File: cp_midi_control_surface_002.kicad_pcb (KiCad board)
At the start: 2 copper layers, 201 parts, among them P1 Power, P10 Guide, P11 Guide, P12 Guide, P13 Guide, P2 Analogue, P3 Digital, P4 Communication, P5 PWM, P6 PWM, P8 Guide, P9 Guide, SW1 B3F-5050, SW10 B3F-5050, SW11 B3F-5050, SW12 B3F-5050, SW13 B3F-5050, SW14 B3F-5050, SW15 B3F-5050, SW16 B3F-5050, SW17 B3F-5050, SW18 B3F-5050, SW19 B3F-5050, SW2 B3F-5050, SW20 B3F-5050, SW21 B3F-5050, SW22 B3F-5050, SW23 B3F-5050, SW24 B3F-5050, SW25 B3F-5050, SW26 B3F-5050, SW27 B3F-5050, SW28 B3F-5050, SW29 B3F-5050, SW3 B3F-5050, SW30 B3F-5050, SW31 B3F-5050, SW32 B3F-5050, SW33 B3F-5050, SW34 B3F-5050, SW35 B3F-5050, SW36 B3F-5050, SW37 B3F-5050, SW38 B3F-5050, SW39 B3F-5050, SW4 B3F-5050, SW40 B3F-5050, SW41 B3F-5050, SW42 B3F-5050, SW43 B3F-5050, SW44 B3F-5050, SW45 B3F-5050, SW46 B3F-5050, SW47 B3F-5050, SW48 B3F-5050, SW49 B3F-5050, SW5 B3F-5050, SW50 B3F-5050, SW51 B3F-5050, SW52 B3F-5050, SW53 B3F-5050, SW54 B3F-5050, SW55 B3F-5050, SW56 B3F-5050, SW6 B3F-5050, SW7 B3F-5050, SW8 B3F-5050, SW9 B3F-5050, U1 CD74HC4067M, U2 CD74HC4067M, U3 CD74HC4067M, U4 CD74HC4067M, U5 CD74HC4067M, U6 CD74HC4067M

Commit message: Resize boards and update connector
Resized the boards to fit the new modular height and started changing the interboard connectors
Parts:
- removed H1, H10, H11, H12, H13, H14, H15, H16, H17, H18, H19, H2, H20, H21, H22, H23, H24, H25, H26, H3, H4, H5, H6, H7, H8, H9: ~, cunabulapress-footprints:Mounting_Hole_M3_with_Target
- removed P10: Guide, cunabulapress-footprints:Mounting_Hole_M3_Target_Only
- removed REF**: Clearance_Hole_M3, cunabulapress-footprints:Clearance_Hole_M3
- removed REF** (x4): Mounting_Hole_M3, cunabulapress-footprints:Mounting_Hole_M3_Target_Only
- J3: footprint cunabulapress-footprints:Connector_TE_Connectivity_Micro-MaTch_8_Position_Female -> Connector_PinHeader_2.54mm:PinHeader_1x06_P2.54mm_Vertical
- moved J3 26.4 mm to (210.4, 225.5), turned to 90 degrees

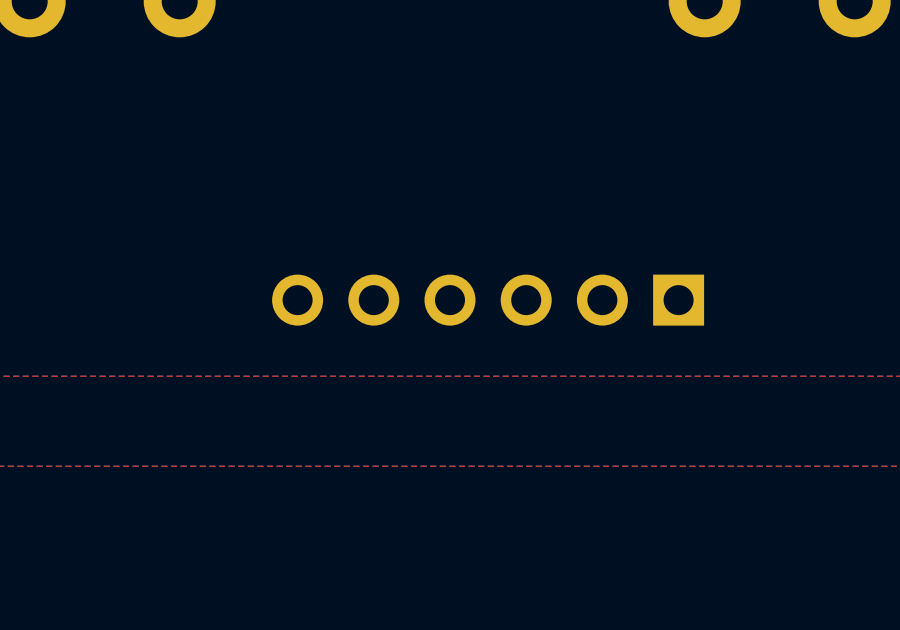
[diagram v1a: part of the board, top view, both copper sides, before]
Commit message: Added Rails to Layout
Found a big problem that the rails are compatible with the boards being modular the way the components are currently spaced.

Which is a little frustrating.
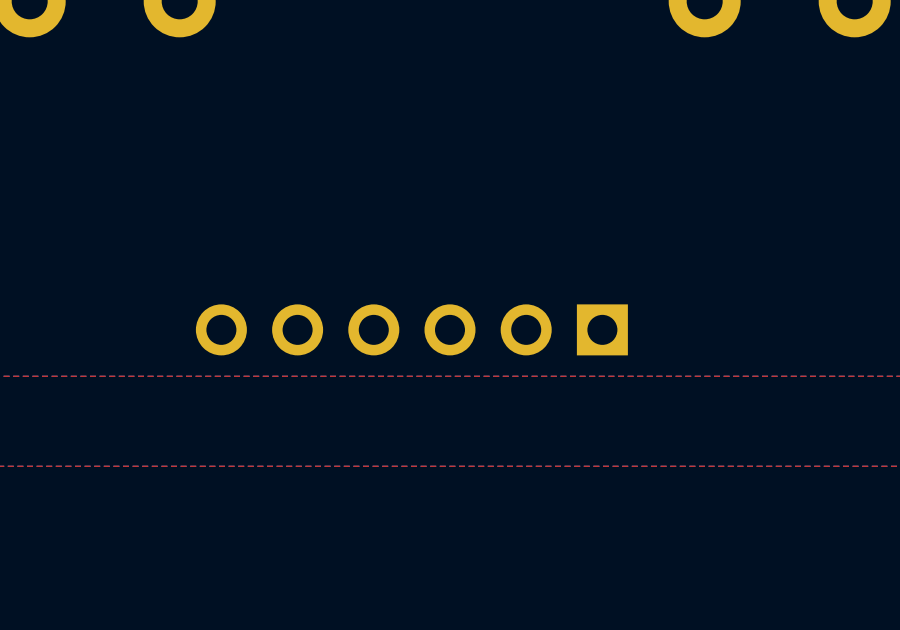
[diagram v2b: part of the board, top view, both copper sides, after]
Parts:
- moved J3 2.73 mm to (207.8, 226.5)

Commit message: COrrected the placement of most of the components for the modular design
Need to finalise the Arduino placement and work out the design for possible extensions.
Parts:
- removed J1, J2, J4, J5, J6, J7, J8: ~, cunabulapress-footprints:Connector_TE_Connectivity_Micro-MaTch_8_Position_Female
- removed J10, J12: ~, Connector_PinSocket_2.54mm:PinSocket_1x04_P2.54mm_Vertical
- removed J11, J9: ~, Connector_PinHeader_2.54mm:PinHeader_1x04_P2.54mm_Vertical
- removed J13, J15, J17, J19: ~, Connector_PinHeader_2.54mm:PinHeader_1x01_P2.54mm_Vertical
- removed J14, J16, J18, J20: ~, Connector_PinSocket_2.54mm:PinSocket_1x01_P2.54mm_Vertical
- removed J21, J23, J25, J27: ~, Connector_PinHeader_2.54mm:PinHeader_1x08_P2.54mm_Vertical
- removed J22, J24, J26, J28: ~, Connector_PinSocket_2.54mm:PinSocket_1x08_P2.54mm_Vertical
- removed J3: ~, Connector_PinHeader_2.54mm:PinHeader_1x06_P2.54mm_Vertical
- removed RN2, RN3: 680Ω (Bussed), Resistor_THT:R_Array_SIP9
- moved RN1 353.4 mm to (791.1, 328.0)
- moved SW_F1 353.4 mm to (768.2, 339.4)
- moved SW36 221.1 mm to (114.3, 264.2)
- moved SW35 220.8 mm to (137.2, 264.2)
- moved SW33 220.3 mm to (182.9, 264.2)
- moved SW40 220.0 mm to (205.7, 264.2)
- moved SW39 219.8 mm to (228.6, 264.2)
- moved SW34 219.7 mm to (160.0, 264.2)
- moved SW38 219.5 mm to (251.5, 264.2)
- moved SW37 219.3 mm to (274.3, 264.2)
- moved D16 188.4 mm to (393.7, 264.2)
- moved D15 188.3 mm to (388.1, 264.2)
- moved D14 188.3 mm to (382.5, 264.2)
- moved D13 188.2 mm to (376.9, 264.2)
- moved D12 188.2 mm to (371.3, 264.2)
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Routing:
- net +5V: track 2702.6 -> 0.00 mm, vias 1 -> 0
- net S3: track 522.6 -> 0.00 mm, vias 1 -> 0
- net S2: track 519.4 -> 0.00 mm, vias 1 -> 0
- net S0: track 516.2 -> 0.00 mm, vias 1 -> 0
- net S1: track 514.1 -> 0.00 mm, vias 1 -> 0
- net Net-(RV3-Pad2): track 481.2 -> 0.00 mm
- net Net-(RV2-Pad2): track 441.6 -> 0.00 mm, vias 1 -> 0
- net Net-(RV8-Pad2): track 401.0 -> 0.00 mm, vias 1 -> 0
- net Net-(RV7-Pad2): track 393.9 -> 0.00 mm, vias 1 -> 0
- net Net-(RV1-Pad2): track 391.8 -> 0.00 mm, vias 1 -> 0
- net Net-(RV6-Pad2): track 390.9 -> 0.00 mm, vias 1 -> 0
- net Net-(RV5-Pad2): track 389.5 -> 0.00 mm, vias 1 -> 0
- net Net-(RV4-Pad2): track 387.1 -> 0.00 mm, vias 1 -> 0
- net /13: track 369.0 -> 0.00 mm
- net /12: track 360.9 -> 0.00 mm
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- removed copper zone on B.Cu, net (none)
- removed copper zone on F.Cu, net (none)
- removed copper zone on B.Cu, net GND
- removed copper zone on F.Cu, net GND
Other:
- board outline added: 421.6 x 221 mm
- board text removed: "Alt Switch position"
- board text removed: "Traces only inside Box"

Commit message: Further cleanup and placement
Removed all the connectors to the rails as they're irrelevant to the top boards.

Added all the support headers.

Need to work out the correct routing for the headers but the placement is correct.
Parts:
- added J1: Conn_02x05_Odd_Even, Connector_PinHeader_2.54mm:PinHeader_2x05_P2.54mm_Vertical, B.Cu at (179.1, 245.1)
- added J2: Conn_02x05_Odd_Even, Connector_PinHeader_2.54mm:PinHeader_2x05_P2.54mm_Vertical, B.Cu at (270.5, 245.1)
- added J5: ~, Connector_PinHeader_2.54mm:PinHeader_2x03_P2.54mm_Vertical, B.Cu at (382.3, 245.1)
- added J7: Conn_02x05_Odd_Even, Connector_PinHeader_2.54mm:PinHeader_2x05_P2.54mm_Vertical, B.Cu at (494.0, 245.1)
- added JA2: ~, Connector_PinHeader_2.54mm:PinHeader_2x03_P2.54mm_Vertical, B.Cu at (382.3, 257.8)
- added JA4: ~, Connector_PinHeader_2.54mm:PinHeader_2x03_P2.54mm_Vertical, B.Cu at (179.1, 257.8)
- added JA6: ~, Connector_PinHeader_2.54mm:PinHeader_2x03_P2.54mm_Vertical, B.Cu at (270.5, 257.8)
- added JA8: ~, Connector_PinHeader_2.54mm:PinHeader_2x03_P2.54mm_Vertical, B.Cu at (494.0, 257.8)
- added JX01: Conn_02x03_Odd_Even, Connector_PinHeader_2.54mm:PinHeader_2x03_P2.54mm_Vertical, B.Cu at (123.2, 146.1)
- added JX02: Conn_02x03_Odd_Even, Connector_PinHeader_2.54mm:PinHeader_2x03_P2.54mm_Vertical, B.Cu at (179.1, 146.1)
- added JX03: Conn_02x03_Odd_Even, Connector_PinHeader_2.54mm:PinHeader_2x03_P2.54mm_Vertical, B.Cu at (123.2, 245.1)
- added JX04: Conn_02x03_Odd_Even, Connector_PinHeader_2.54mm:PinHeader_2x03_P2.54mm_Vertical, B.Cu at (214.6, 146.1)
- added JX05: Conn_02x03_Odd_Even, Connector_PinHeader_2.54mm:PinHeader_2x03_P2.54mm_Vertical, B.Cu at (270.5, 146.1)
- added JX06: Conn_02x03_Odd_Even, Connector_PinHeader_2.54mm:PinHeader_2x03_P2.54mm_Vertical, B.Cu at (214.6, 245.1)
- added JX07: Conn_02x03_Odd_Even, Connector_PinHeader_2.54mm:PinHeader_2x03_P2.54mm_Vertical, B.Cu at (326.4, 146.1)
- added JX08: Conn_02x03_Odd_Even, Connector_PinHeader_2.54mm:PinHeader_2x03_P2.54mm_Vertical, B.Cu at (382.3, 146.1)
- added JX09: Conn_02x03_Odd_Even, Connector_PinHeader_2.54mm:PinHeader_2x03_P2.54mm_Vertical, B.Cu at (326.4, 245.1)
- added JX10: Conn_02x03_Odd_Even, Connector_PinHeader_2.54mm:PinHeader_2x03_P2.54mm_Vertical, B.Cu at (438.1, 146.1)
- added JX11: Conn_02x03_Odd_Even, Connector_PinHeader_2.54mm:PinHeader_2x03_P2.54mm_Vertical, B.Cu at (494.0, 146.1)
- added JX12: Conn_02x03_Odd_Even, Connector_PinHeader_2.54mm:PinHeader_2x03_P2.54mm_Vertical, B.Cu at (438.1, 245.1)
- added JX13: Conn_02x03_Odd_Even, Connector_PinHeader_2.54mm:PinHeader_2x03_P2.54mm_Vertical, B.Cu at (123.2, 257.8)
- added JX14: Conn_02x03_Odd_Even, Connector_PinHeader_2.54mm:PinHeader_2x03_P2.54mm_Vertical, B.Cu at (214.6, 257.8)
- added JX15: Conn_02x03_Odd_Even, Connector_PinHeader_2.54mm:PinHeader_2x03_P2.54mm_Vertical, B.Cu at (326.4, 257.8)
- added JX16: Conn_02x03_Odd_Even, Connector_PinHeader_2.54mm:PinHeader_2x03_P2.54mm_Vertical, B.Cu at (438.1, 257.8)
- added JX17: Conn_02x03_Odd_Even, Connector_PinHeader_2.54mm:PinHeader_2x03_P2.54mm_Vertical, B.Cu at (123.2, 356.9)
- added JX18: Conn_02x03_Odd_Even, Connector_PinHeader_2.54mm:PinHeader_2x03_P2.54mm_Vertical, B.Cu at (179.1, 356.9)
- added JX19: Conn_02x03_Odd_Even, Connector_PinHeader_2.54mm:PinHeader_2x03_P2.54mm_Vertical, B.Cu at (214.6, 356.9)
- added JX20: Conn_02x03_Odd_Even, Connector_PinHeader_2.54mm:PinHeader_2x03_P2.54mm_Vertical, B.Cu at (270.5, 356.9)
- added JX21: Conn_02x03_Odd_Even, Connector_PinHeader_2.54mm:PinHeader_2x03_P2.54mm_Vertical, B.Cu at (326.4, 356.9)
- added JX22: Conn_02x03_Odd_Even, Connector_PinHeader_2.54mm:PinHeader_2x03_P2.54mm_Vertical, B.Cu at (382.3, 356.9)
- added JX23: Conn_02x03_Odd_Even, Connector_PinHeader_2.54mm:PinHeader_2x03_P2.54mm_Vertical, B.Cu at (438.1, 356.9)
- added JX24: Conn_02x03_Odd_Even, Connector_PinHeader_2.54mm:PinHeader_2x03_P2.54mm_Vertical, B.Cu at (494.0, 356.9)
- added J_EXT_1: Conn_01x10, Connector_PinSocket_2.54mm:PinSocket_1x09_P2.54mm_Vertical, F.Cu at (520.7, 274.3)
- added RN2: 680Ω (Bussed), Resistor_THT:R_Array_SIP9, F.Cu at (309.9, 270.5)
- added RN3: 680Ω (Bussed), Resistor_THT:R_Array_SIP9, F.Cu at (373.4, 270.5)
- P3: footprint Connector_PinHeader_2.54mm:PinHeader_1x18_P2.54mm_Vertical -> Connector_PinHeader_2.54mm:PinHeader_2x18_P2.54mm_Vertical
- moved RN1 587.8 mm to (205.8, 274.3)
- moved SW_F1 587.8 mm to (182.9, 285.7)
- moved U5 176.8 mm to (291.1, 320.0), turned to 0 degrees
- moved P3 146.6 mm to (419.1, 299.7)
- moved P11 146.3 mm to (497.8, 342.9)
- moved P13 146.3 mm to (422.9, 342.9)
- moved P4 146.3 mm to (444.5, 342.9)
- moved P5 146.3 mm to (467.4, 342.9)
- moved P6 146.3 mm to (494.3, 342.9)
- moved P1 146.3 mm to (485.1, 294.6)
- moved P12 146.3 mm to (447.0, 327.7)
- moved P2 146.3 mm to (462.3, 294.6)
- moved P8 146.3 mm to (499.1, 294.6)
- moved P9 146.3 mm to (447.0, 299.7)
- turned SW_1 to 0 degrees
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- renumbered PT_2 to PT_1, PT_16 to PT_15, PT_15 to PT_16, PT_1 to PT_2, SW36 to SW_1, SW35 to SW_2, SW34 to SW_3, SW33 to SW_4, SW40 to SW_5, SW39 to SW_6, SW38 to SW_7, SW37 to SW_8
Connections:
- D1 pad 2: Net-(D1-Pad2) -> /17
- D10 pad 2: Net-(D10-Pad2) -> /7
- D11 pad 2: Net-(D11-Pad2) -> /8
- D12 pad 2: Net-(D12-Pad2) -> /9
- D13 pad 2: Net-(D13-Pad2) -> /10
- D14 pad 2: Net-(D14-Pad2) -> /11
- D15 pad 2: Net-(D15-Pad2) -> /12
- D16 pad 2: Net-(D16-Pad2) -> /13
- D2 pad 2: Net-(D2-Pad2) -> /16
- D3 pad 2: Net-(D3-Pad2) -> /15
- D4 pad 2: Net-(D4-Pad2) -> /14
- D5 pad 2: Net-(D5-Pad2) -> /2
- D6 pad 2: Net-(D6-Pad2) -> /3
- D7 pad 2: Net-(D7-Pad2) -> /4
- D8 pad 2: Net-(D8-Pad2) -> /5
- D9 pad 2: Net-(D9-Pad2) -> /6
- P3 pad 10: /37 -> /47
- P3 pad 11: /35 -> Net-(P3-Pad11)
- P3 pad 12: Net-(P3-Pad12) -> /45
- P3 pad 14: S2 -> /43
- P3 pad 15: S3 -> Net-(P3-Pad15)
- P3 pad 16: S1 -> /41
- P3 pad 17: S0 -> Net-(P3-Pad17)
- P3 pad 18: +5V -> /39
- P3 pad 2: /53 -> GND
- P3 pad 3: /51 -> Net-(P3-Pad3)
- P3 pad 4: /49 -> /53
- P3 pad 5: /47 -> Net-(P3-Pad5)
- P3 pad 6: /45 -> /51
- P3 pad 7: /43 -> Net-(P3-Pad7)
- P3 pad 8: /41 -> /49
- P3 pad 9: /39 -> Net-(P3-Pad9)
- PT_1 pad 2: Net-(PT_2-Pad2) -> Net-(PT_1-Pad2)
- PT_15 pad 2: Net-(PT_16-Pad2) -> Net-(PT_15-Pad2)
- PT_16 pad 2: Net-(PT_15-Pad2) -> Net-(PT_16-Pad2)
- PT_2 pad 2: Net-(PT_1-Pad2) -> Net-(PT_2-Pad2)
- RN8 pad 1: GND -> Net-(RN8-Pad1)
- RN9 pad 1: GND -> Net-(RN8-Pad1)
- U5 pad 16: Net-(U5-Pad16) -> Net-(RVM1-Pad2)
- U5 pad 23: Net-(RVM1-Pad2) -> Net-(J_EXT_1-Pad2)
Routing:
- net +5V: track 0.00 -> 1069.6 mm
- net Net-(PT_6-Pad2): track 0.00 -> 69.9 mm
- net Net-(PT_7-Pad2): track 0.00 -> 67.0 mm
- net Net-(PT_11-Pad2): track 0.00 -> 67.0 mm
- net Net-(PT_10-Pad2): track 0.00 -> 59.7 mm
- net Net-(PT_3-Pad2): track 0.00 -> 57.0 mm
- net Net-(PT_14-Pad2): track 0.00 -> 53.9 mm
- net Net-(PT_12-Pad2): track 0.00 -> 53.7 mm
- net Net-(PT_5-Pad2): track 0.00 -> 45.1 mm
- net Net-(PT_13-Pad2): track 0.00 -> 42.2 mm
- net Net-(PT_4-Pad2): track 0.00 -> 40.4 mm
- net Net-(PT_16-Pad2): track 0.00 -> 36.0 mm
- net Net-(PT_1-Pad2): track 0.00 -> 36.0 mm
- net Net-(PT_9-Pad2): track 0.00 -> 21.2 mm
- net Net-(PT_8-Pad2): track 0.00 -> 19.5 mm
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- added copper zone on B.Cu, net GND
- added copper zone on F.Cu, net GND

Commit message: Forgot to update a couple of components
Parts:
- JA4, JA6: footprint Connector_PinHeader_2.54mm:PinHeader_2x03_P2.54mm_Vertical -> Connector_PinHeader_2.54mm:PinHeader_2x05_P2.54mm_Vertical

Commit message: Moved two overlapping boards out of the way for clarity and cleaned up folder
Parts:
- moved RN1 307.6 mm to (513.1, 287.0)
- moved SW_F1 307.6 mm to (490.2, 298.4)
- moved J1 111.8 mm to (179.1, 133.3)
- moved J2 111.8 mm to (270.5, 133.3)
- moved JX01 111.8 mm to (123.2, 34.3)
- moved JX02 111.8 mm to (179.1, 34.3)
- moved JX03 111.8 mm to (123.2, 133.3)
- moved JX04 111.8 mm to (214.6, 34.3)
- moved JX05 111.8 mm to (270.5, 34.3)
- moved JX06 111.8 mm to (214.6, 133.3)
- moved SW11 111.8 mm to (114.3, 48.3)
- moved SW22 111.8 mm to (274.3, 48.3)
- moved SW24 111.8 mm to (251.5, 48.3)
- moved SW25 111.8 mm to (228.6, 48.3)
- moved SW27 111.8 mm to (205.7, 48.3)
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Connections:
- RN3 pad 2: Net-(D9-Pad1) -> Net-(D16-Pad1)
- RN3 pad 3: Net-(D10-Pad1) -> Net-(D15-Pad1)
- RN3 pad 4: Net-(D11-Pad1) -> Net-(D14-Pad1)
- RN3 pad 5: Net-(D12-Pad1) -> Net-(D13-Pad1)
- RN3 pad 6: Net-(D13-Pad1) -> Net-(D12-Pad1)
- RN3 pad 7: Net-(D14-Pad1) -> Net-(D11-Pad1)
- RN3 pad 8: Net-(D15-Pad1) -> Net-(D10-Pad1)
- RN3 pad 9: Net-(D16-Pad1) -> Net-(D9-Pad1)
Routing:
- net +5V: track 1069.6 -> 1418.8 mm
- net Net-(J5-Pad5): track 0.00 -> 87.8 mm, vias 0 -> 1
- net Net-(J5-Pad1): track 0.00 -> 66.5 mm
- net Net-(J5-Pad3): track 0.00 -> 66.2 mm
- net Net-(J5-Pad4): track 0.00 -> 65.8 mm
- net Net-(J5-Pad2): track 0.00 -> 61.6 mm
- net Net-(RN5-Pad3): track 0.00 -> 28.8 mm
- net Net-(RN5-Pad2): track 0.00 -> 9.95 mm
- net Net-(PT_7-Pad2): track 67.0 -> 57.9 mm
- net Net-(PT_5-Pad2): track 45.1 -> 51.8 mm
- net Net-(RN1-Pad9): track 3.81 -> 0.00 mm
- net Net-(RN1-Pad8): track 3.81 -> 0.00 mm
- net Net-(RN1-Pad7): track 3.81 -> 0.00 mm
- net Net-(RN1-Pad6): track 3.81 -> 0.00 mm
- net Net-(RN1-Pad5): track 3.81 -> 0.00 mm
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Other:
- board size 421.6 x 221 mm -> 421.6 x 332.7 mm
- board text added: "Traces only"

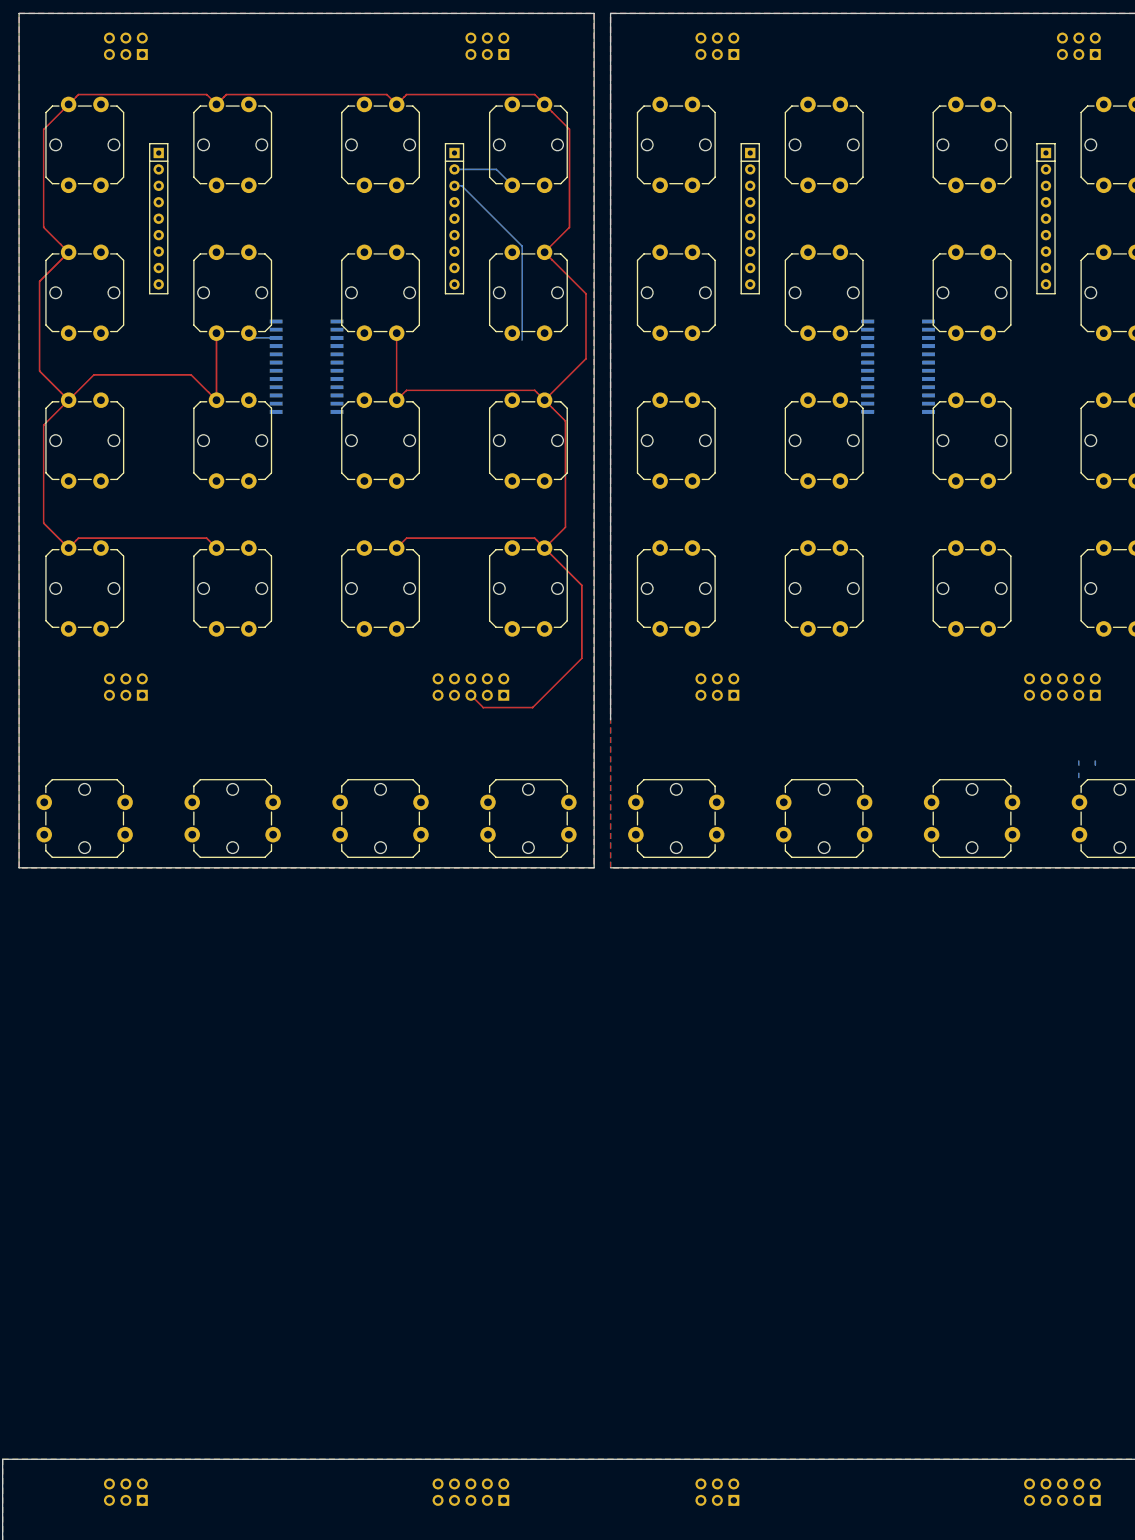
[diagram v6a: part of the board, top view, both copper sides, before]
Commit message: Routing left button blocks (traces for bottom buttons TBD)
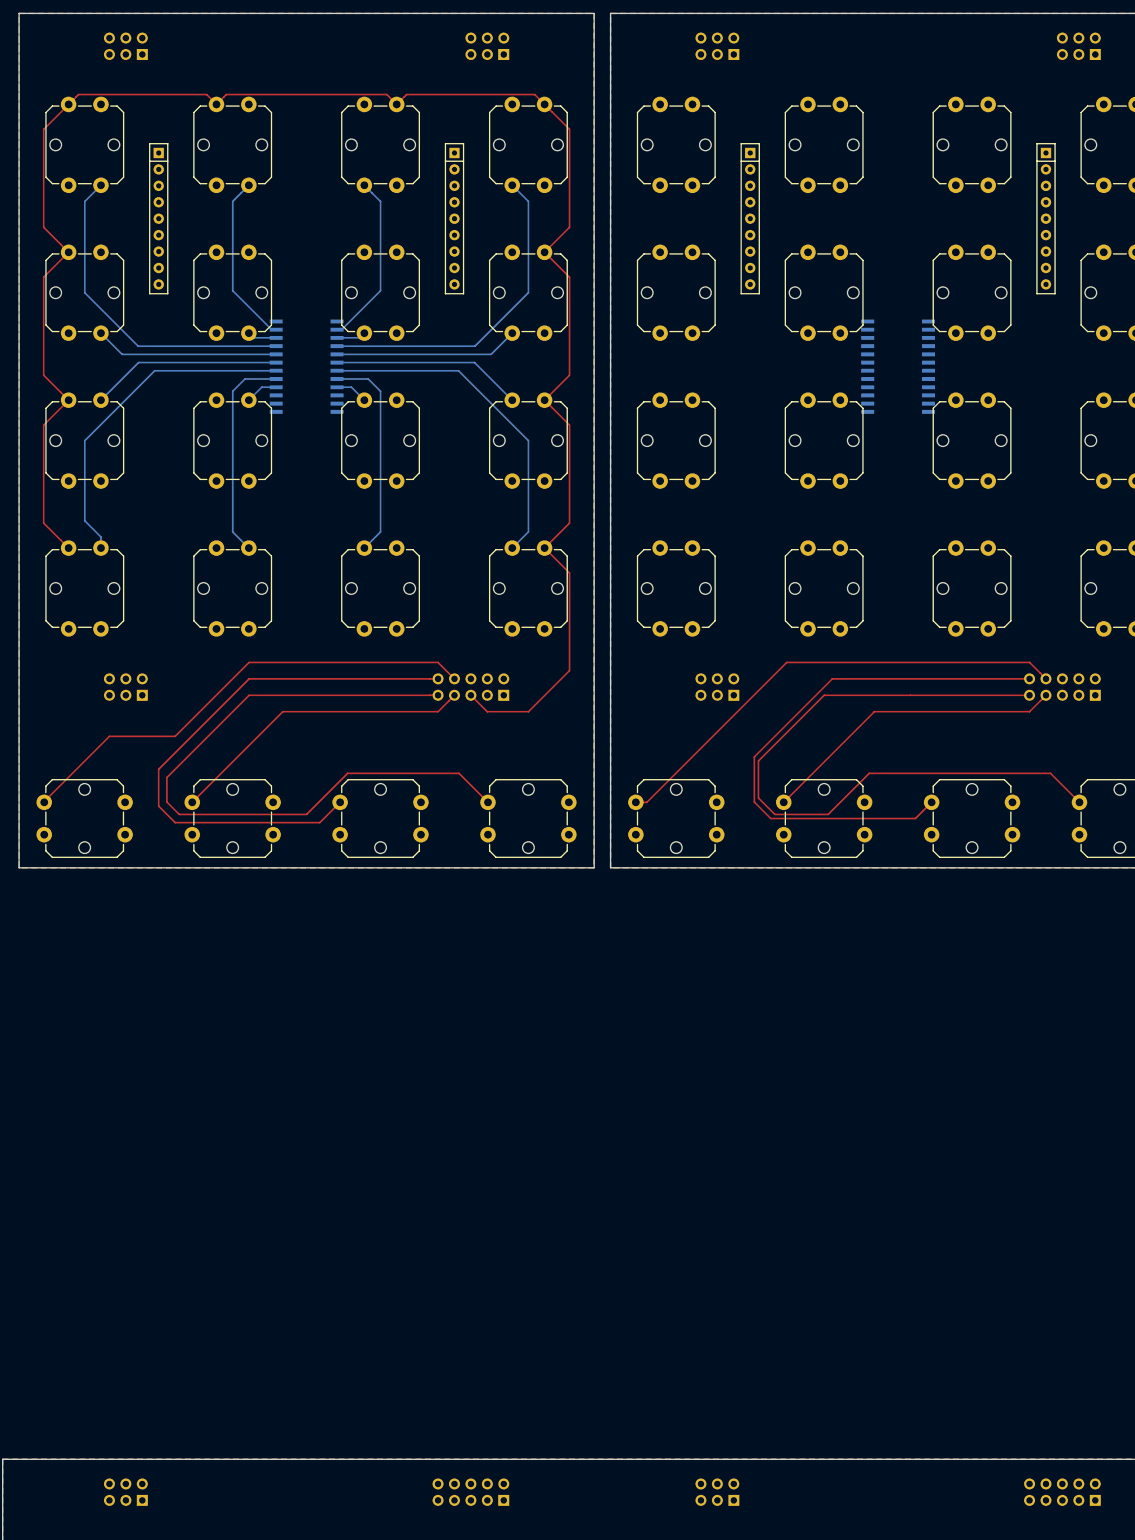
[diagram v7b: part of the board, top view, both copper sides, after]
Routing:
- net +5V: track 1418.8 -> 1296.5 mm
- net Net-(J2-Pad9): track 0.00 -> 107.0 mm
- net Net-(J1-Pad9): track 0.00 -> 105.9 mm
- net Net-(J1-Pad10): track 0.00 -> 85.1 mm
- net Net-(J2-Pad10): track 0.00 -> 84.0 mm
- net Net-(J1-Pad8): track 0.00 -> 73.5 mm
- net Net-(J2-Pad8): track 0.00 -> 73.4 mm
- net Net-(RN5-Pad5): track 0.00 -> 51.7 mm
- net Net-(RN4-Pad5): track 0.00 -> 51.7 mm
- net Net-(RN4-Pad2): track 0.00 -> 50.7 mm
- net Net-(J2-Pad7): track 0.00 -> 47.4 mm
- net Net-(J1-Pad7): track 0.00 -> 47.4 mm
- net Net-(RN5-Pad2): track 9.95 -> 50.7 mm
- net Net-(RN5-Pad9): track 0.00 -> 32.8 mm
- net Net-(RN4-Pad9): track 0.00 -> 32.8 mm
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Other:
- outline, holes or cut-outs redrawn
